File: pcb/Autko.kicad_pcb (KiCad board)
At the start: 2 copper layers, 140 x 155 mm, 123 parts, among them J1 PDI, M1 LEFT, M2 RIGHT, Q1 Si4368DY, Q2 BC817, SW1 POWER, SW2 START, SW3 STOP, U1 LTC3872, U10 CNY70, U11 TB6612FNG, U12 74HC14, U13 RN4678, U2 TLV1117-33, U3 ATxmega16A4U-A, U4 CNY70, U5 CNY70, U6 CNY70, U7 CNY70, U8 CNY70, U9 CNY70, Y1 8MHz

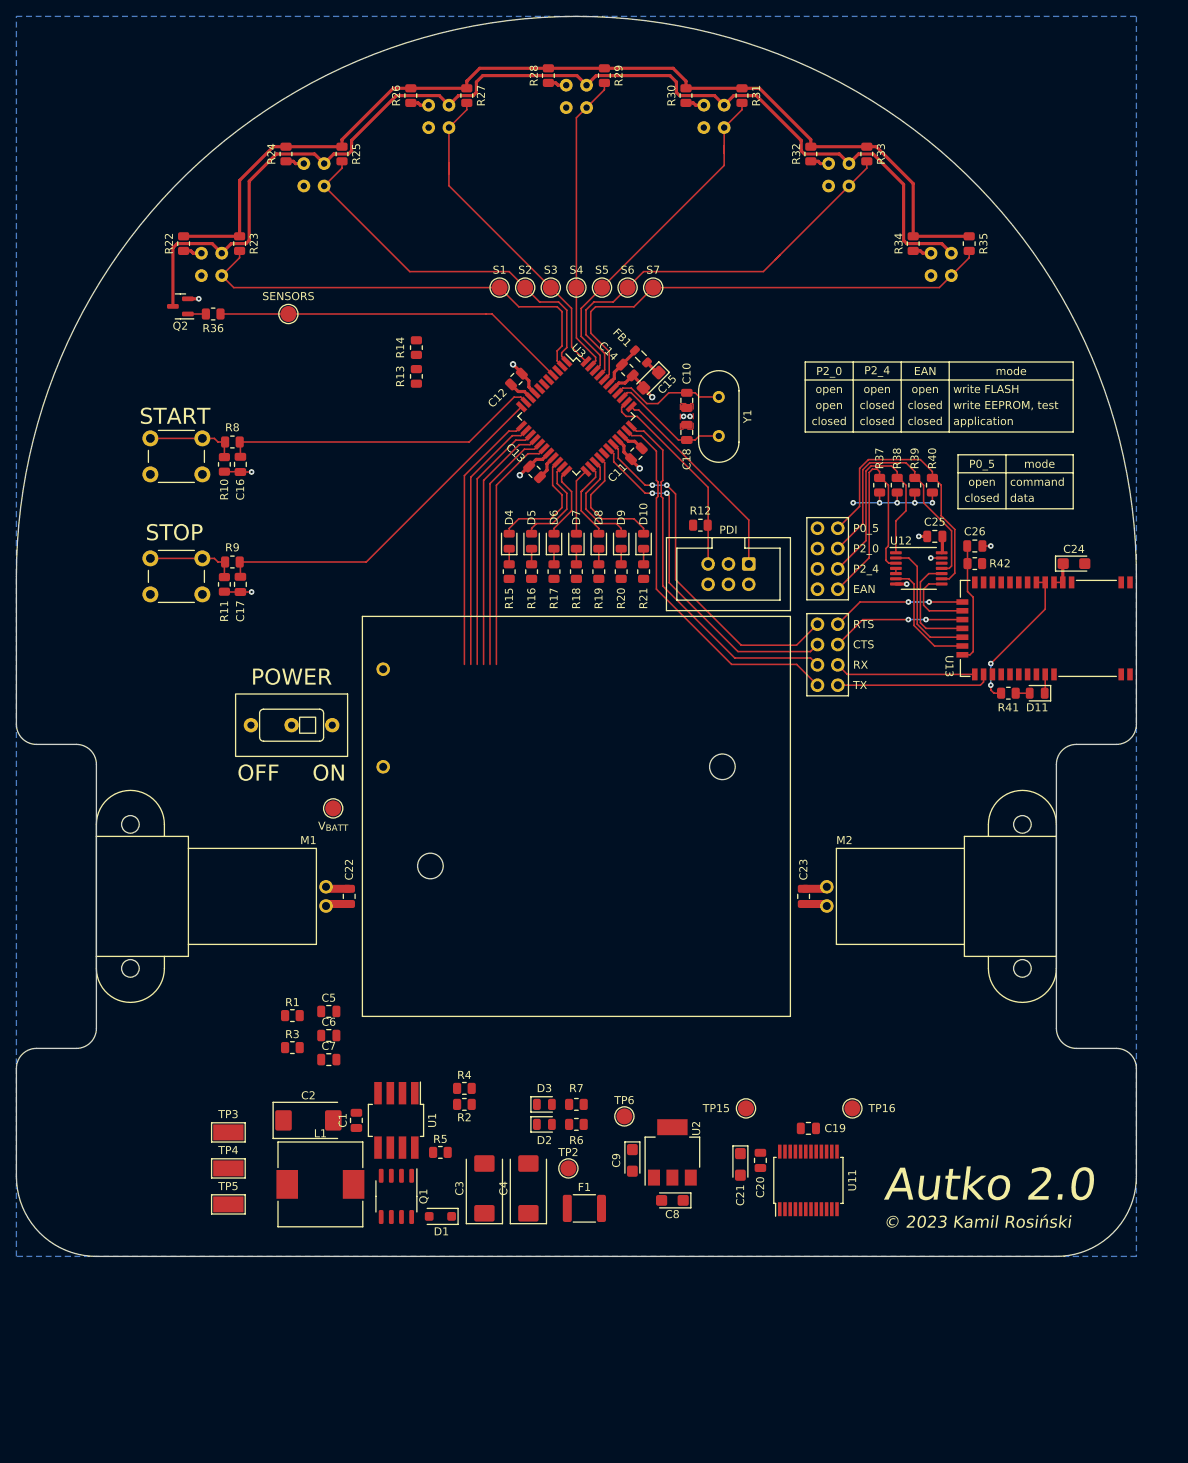
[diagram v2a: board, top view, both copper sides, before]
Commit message: [pcb] Boost converter routing
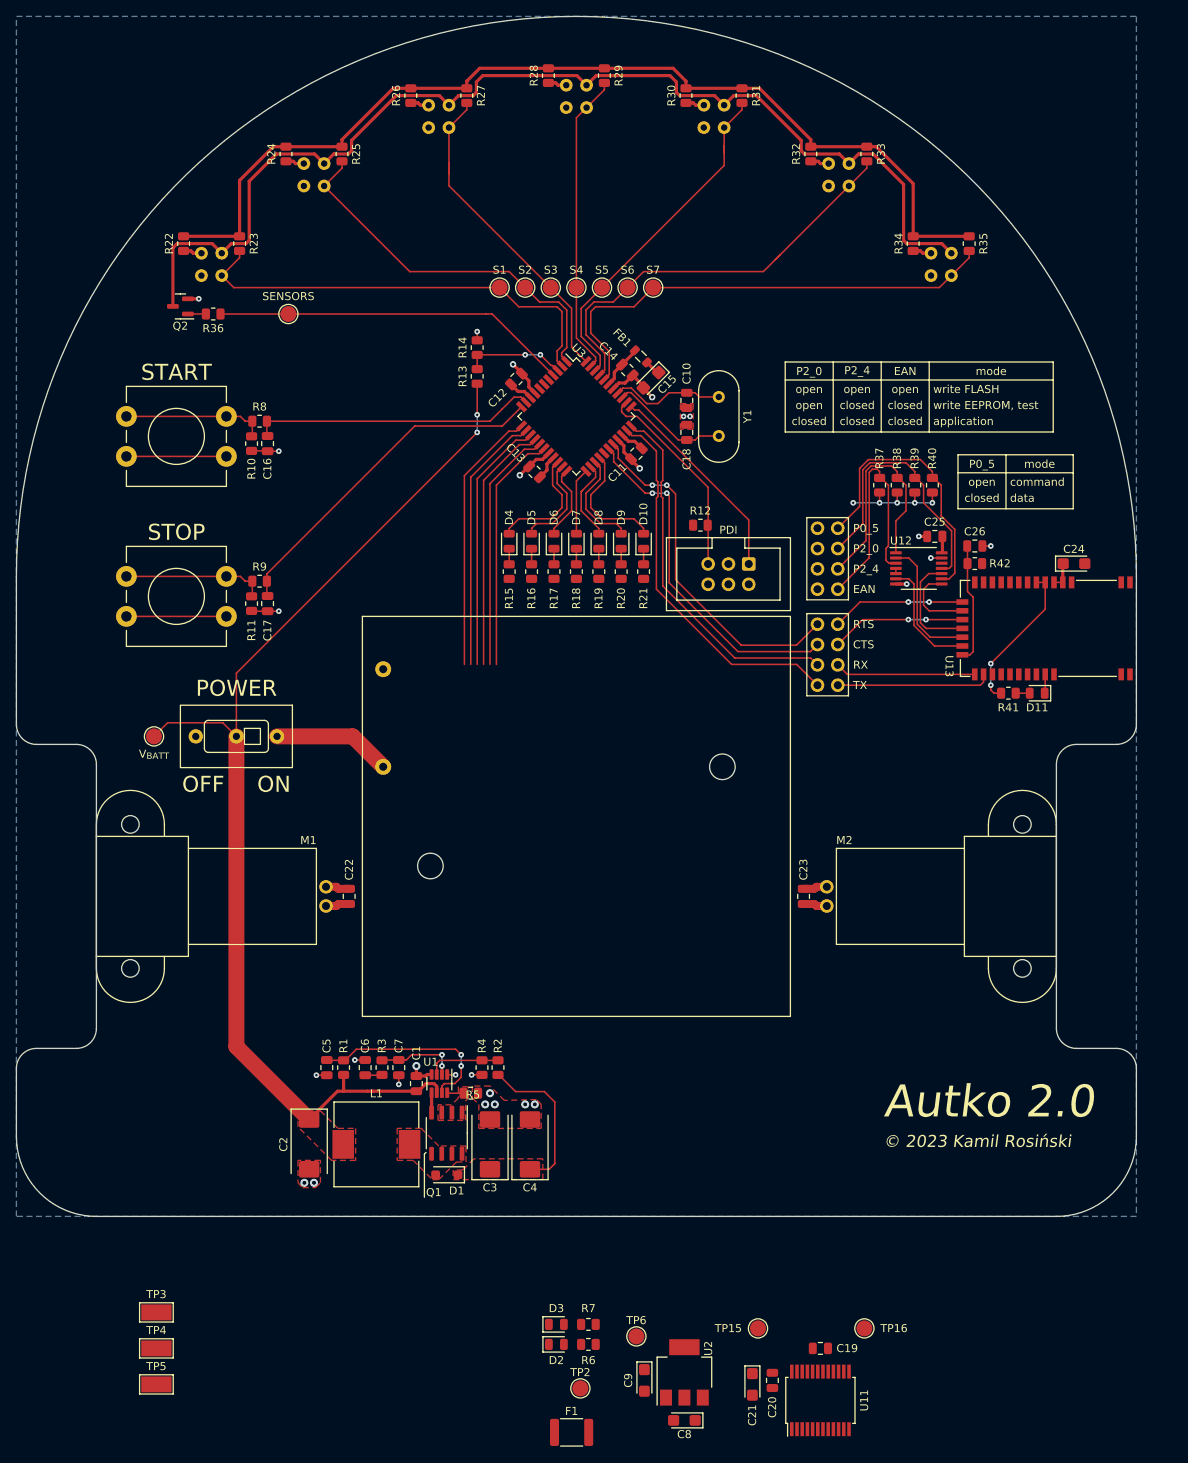
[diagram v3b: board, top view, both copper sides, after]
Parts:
- SW2, SW3: footprint Button_Switch_THT:SW_PUSH_6mm_H5mm -> Autko:12mm_tact_switch
- U1: footprint Package_TO_SOT_SMD:SOT-223-8 -> Package_TO_SOT_SMD:SOT-23-8
- moved F1 28.0 mm to (98.9, 207.5)
- moved C19 27.5 mm to (130.0, 197.0)
- moved C20 27.5 mm to (124.0, 201.0)
- moved C21 27.5 mm to (121.5, 201.5)
- moved C8 27.5 mm to (113.0, 206.0)
- moved C9 27.5 mm to (108.0, 201.0)
- moved D2 27.5 mm to (97.0, 196.5)
- moved D3 27.5 mm to (97.0, 194.0)
- moved R6 27.5 mm to (101.0, 196.5)
- moved R7 27.5 mm to (101.0, 194.0)
- moved TP15 27.5 mm to (122.2, 194.5)
- moved TP16 27.5 mm to (135.5, 194.5)
- moved TP2 27.5 mm to (100.0, 202.0)
- moved TP6 27.5 mm to (107.0, 195.5)
- moved U11 27.5 mm to (130.0, 203.5)
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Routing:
- net +BATT: track 0.00 -> 140.7 mm, vias 0 -> 2
- net +3.3V: track 157.6 -> 182.6 mm
- net Net-(U1-RUN/SS): track 0.00 -> 24.2 mm, vias 0 -> 2
- net Net-(D1-K): track 0.00 -> 19.6 mm
- net Net-(BT1-+): track 0.00 -> 14.8 mm
- net Net-(U3-PA7): track 0.00 -> 12.7 mm, vias 0 -> 2
- net GND: track 34.1 -> 44.5 mm, vias 13 -> 27
- net Net-(U1-ITH): track 0.00 -> 10.2 mm, vias 0 -> 2
- net Net-(U1-FB): track 0.00 -> 9.21 mm
- net Net-(R11-Pad1): track 11.4 -> 17.9 mm
- net Net-(R10-Pad1): track 11.4 -> 17.9 mm
- net /Microcontroller/BTN_START: track 40.3 -> 35.8 mm
- net Net-(Q1-G): track 0.00 -> 2.49 mm
- net Net-(C6-Pad1): track 0.00 -> 2.12 mm
- net Net-(U1-SW): track 0.00 -> 1.94 mm
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- added copper zone on F.Cu, net +BATT
- added copper zone on F.Cu, net Net-(D1-A)
- added copper zone on F.Cu, net Net-(D1-K)
- added copper zone on F.Cu, net Net-(U1-SW)
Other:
- board size 140 x 155 mm -> 140 x 150 mm

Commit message: [pcb] Voltage regulator and motor driver
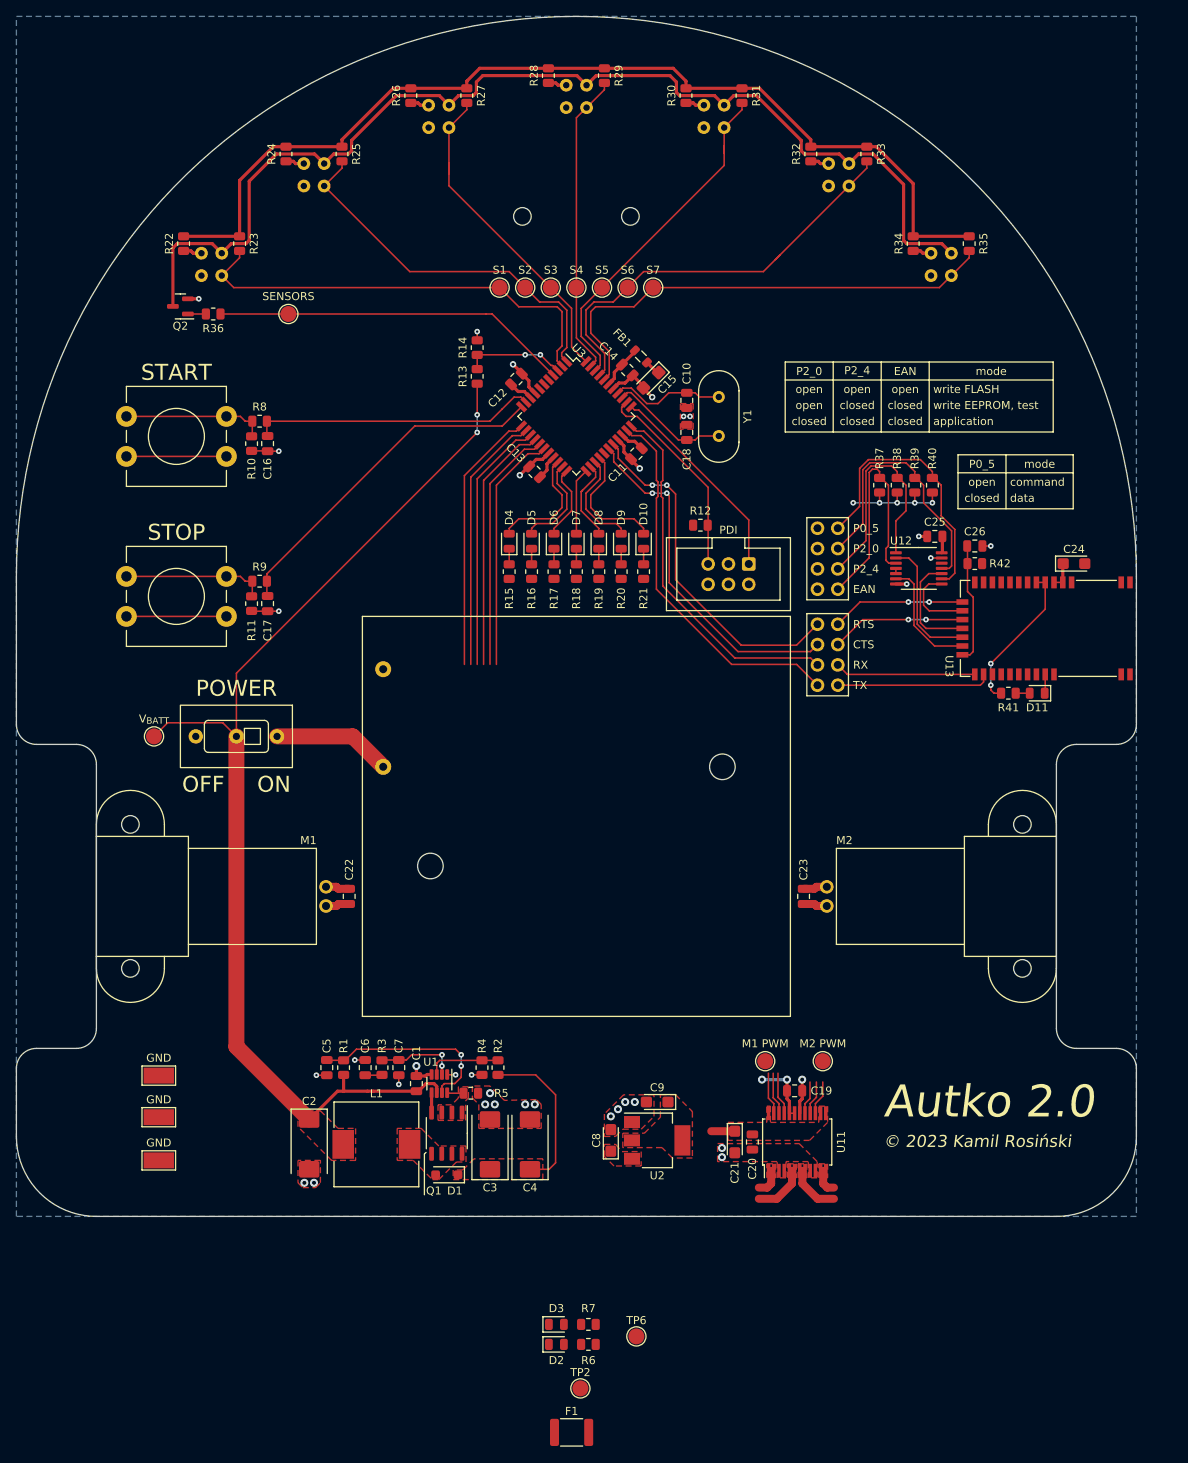
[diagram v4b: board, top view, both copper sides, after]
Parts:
- added REF**: Pololu_ball_caster, Autko:Pololu_ball_caster, F.Cu at (99.5, 55.5)
- moved C8 36.2 mm to (103.8, 171.0), turned to 90 degrees
- moved C9 34.8 mm to (109.6, 166.2), turned to 180 degrees
- moved TP16 33.8 mm to (130.3, 161.1)
- moved TP15 33.4 mm to (123.1, 161.1)
- moved TP5 33.4 mm to (47.3, 168.1)
- moved U11 32.4 mm to (127.1, 171.2)
- moved C19 32.4 mm to (126.8, 164.8)
- moved C21 30.4 mm to (119.3, 171.2)
- moved C20 29.9 mm to (121.5, 171.2)
- moved TP3 29.6 mm to (47.3, 162.9)
- moved U2 29.2 mm to (109.6, 171.0), turned to 0 degrees
- moved TP4 23.5 mm to (47.3, 173.5)
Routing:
- net +3.3V: track 182.6 -> 190.7 mm, vias 5 -> 7
- net Net-(M1--): track 3.36 -> 9.89 mm
- net Net-(M2--): track 3.36 -> 9.69 mm
- net /Microcontroller/M1_IN1: track 32.1 -> 37.5 mm
- net /Microcontroller/M1_IN2: track 32.7 -> 38.0 mm
- net /Microcontroller/M1_PWM: track 33.3 -> 38.6 mm
- net GND: track 44.5 -> 48.9 mm, vias 27 -> 34
- net /Microcontroller/M2_PWM: track 30.3 -> 34.5 mm
- net /Microcontroller/M2_IN2: track 30.8 -> 35.1 mm
- net /Microcontroller/M2_IN1: track 31.6 -> 35.7 mm
- net Net-(M1-+): track 3.36 -> 6.71 mm
- net Net-(M2-+): track 3.36 -> 6.51 mm
- net +7.5V: track 0.00 -> 2.95 mm
- net Net-(D1-K): track 19.6 -> 20.3 mm
- added copper zone on F.Cu, net +3.3V
- added copper zone on F.Cu, net +7.5V
- added copper zone on F.Cu, net Net-(M1-+)
- added copper zone on F.Cu, net Net-(M1--)
- added copper zone on F.Cu, net Net-(M2-+)
- added copper zone on F.Cu, net Net-(M2--)

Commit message: [pcb] Bluetooth ground plane
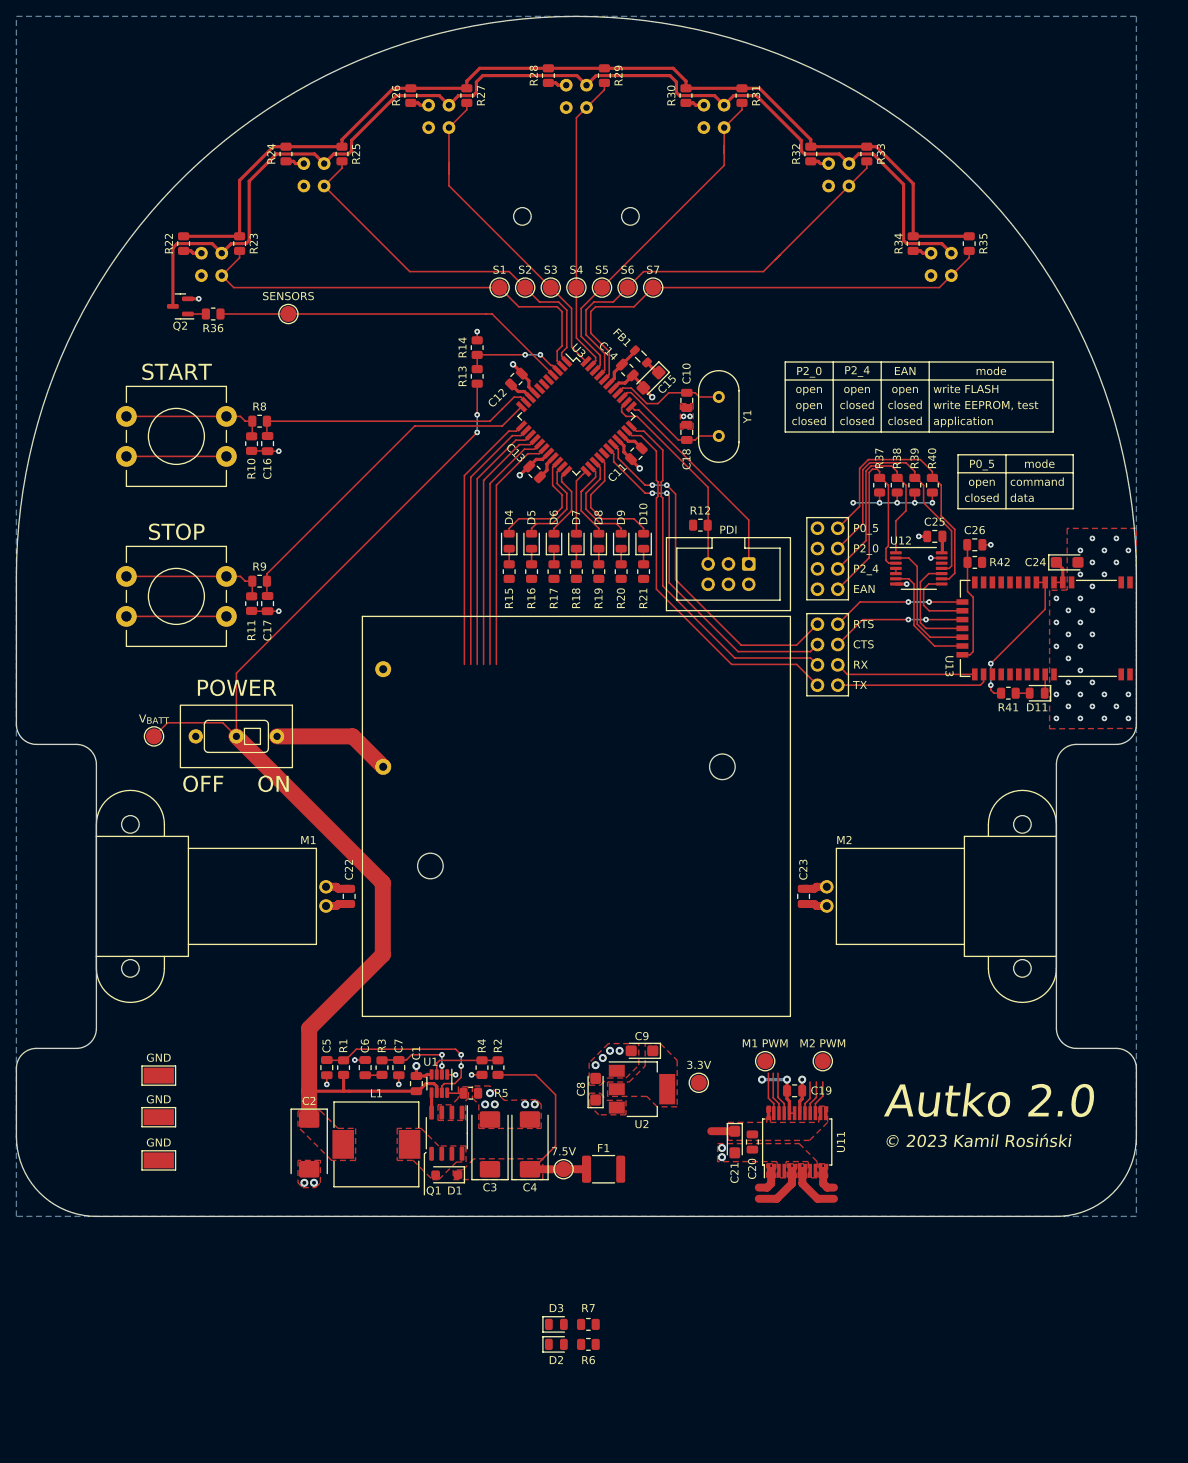
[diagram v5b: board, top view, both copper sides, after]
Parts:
- moved F1 33.1 mm to (102.9, 174.6)
- moved TP6 32.6 mm to (114.8, 163.8)
- moved TP2 27.5 mm to (97.9, 174.6)
- moved C8 6.68 mm to (101.9, 164.6)
- moved U2 6.68 mm to (107.7, 164.6)
- moved C9 6.68 mm to (107.7, 159.8)
- moved C24 0.86 mm to (160.8, 98.8)
- moved C26 0.15 mm to (149.3, 96.5)
- moved R42 0.15 mm to (149.3, 98.8)
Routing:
- net +BATT: track 140.7 -> 146.9 mm
- net Net-(D1-K): track 20.3 -> 26.1 mm
- net GND: track 48.9 -> 48.7 mm, vias 34 -> 69

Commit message: [pcb] Some power routing
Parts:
- moved R6 36.0 mm to (101.3, 160.5), turned to 90 degrees
- moved R7 33.8 mm to (105.3, 160.5), turned to 90 degrees
- moved D2 32.7 mm to (101.3, 164.1), turned to -90 degrees
- moved D3 31.0 mm to (105.3, 164.1), turned to -90 degrees
- moved TP6 10.2 mm to (105.3, 167.5)
- moved TP2 7.87 mm to (101.3, 167.5)
- moved C9 7.42 mm to (115.1, 159.3)
- moved C8 7.42 mm to (109.3, 164.1)
- moved U2 7.42 mm to (115.1, 164.1)
- moved TP15 2.98 mm to (125.5, 159.3)
- moved C2 2.69 mm to (67.9, 169.5)
- moved C6 2.69 mm to (74.9, 159.9)
- moved C1 2.69 mm to (81.3, 161.9)
- moved C3 2.69 mm to (90.5, 169.5)
- moved C4 2.69 mm to (95.5, 169.5)
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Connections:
- D2 pad 1: GND -> Net-(D2-K)
- D2 pad 2: Net-(D2-A) -> +7.5V
- D3 pad 1: GND -> Net-(D3-K)
- D3 pad 2: Net-(D3-A) -> +3.3V
- M2 pad 1: Net-(M2-+) -> Net-(M2--)
- M2 pad 2: Net-(M2--) -> Net-(M2-+)
- R6 pad 1: +7.5V -> Net-(D2-K)
- R6 pad 2: Net-(D2-A) -> GND
- R7 pad 1: +3.3V -> Net-(D3-K)
- R7 pad 2: Net-(D3-A) -> GND
- TP2 pad 1: Net-(D1-K) -> +7.5V
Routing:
- net +3.3V: track 191.2 -> 446.6 mm, vias 7 -> 12
- net Net-(M1--): track 9.89 -> 118.2 mm
- net Net-(M1-+): track 6.71 -> 110.1 mm
- net /Microcontroller/M2_IN1: track 35.7 -> 104.0 mm
- net /Microcontroller/M2_IN2: track 35.1 -> 103.3 mm
- net /Microcontroller/M2_PWM: track 34.5 -> 102.6 mm
- net /Microcontroller/M1_IN1: track 37.5 -> 104.5 mm
- net /Microcontroller/M1_IN2: track 38.0 -> 105.0 mm
- net /Microcontroller/M1_PWM: track 38.6 -> 105.5 mm
- net Net-(M2--): track 9.69 -> 49.9 mm
- net +7.5V: track 2.95 -> 37.9 mm
- net Net-(M2-+): track 6.51 -> 39.9 mm
- net Net-(D1-K): track 26.1 -> 21.4 mm
- net +BATT: track 146.9 -> 143.1 mm
- net GND: track 48.7 -> 51.3 mm, vias 69 -> 71
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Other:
- board size 140 x 150 mm -> 140 x 155 mm
